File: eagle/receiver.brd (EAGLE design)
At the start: 68.6 x 53.3 mm, 15 parts, among them IC1 7805T, U1 ARDUINOR3-DIMENSION

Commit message: Better power management, improve usability
- LED strip pins reordered to match most strips
- Added a reset button
- Added a diode to protect the arduino from non-5vdc supplies
- Added a solder jumper to pick between sharing the arduino's 5vdc supply with
  the strip or whatever is on VCC
- Filter cap on regulator circuit
- Documentation silkscreens
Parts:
- added C1: (no value), adafruit:153CLV-0405
- added D1: (no value), adafruit:SMADIODE
- added JP7: (no value), SparkFun:1X02
- added RESET: (no value), SparkFun:TACTILE_SWITCH_SMD
- added U$4: (no value), phrobo:PHROBO-LOGO
- added U$5: (no value), ohw-logo:OSHW_FILLX150_NOTEXT
- added VCC/+5V: NC=+5v, SparkFun:SJ_2S-NO
- moved JP5 9.67 mm to (62.2, 20.3)
- moved JP3 7.73 mm to (62.2, 25.4)
- moved JP4 7.73 mm to (54.6, 25.4)
- moved JP6 7.41 mm to (54.6, 20.3)
- moved JP1 4.02 mm to (62.2, 15.2)
- moved JP2 4.02 mm to (54.6, 15.2)
- moved CLOCK 3.81 mm to (3.81, 47.0)
- moved DATA 3.81 mm to (3.81, 43.2)
- flipped VCC to the top, turned to 270 degrees
- renumbered 5V to +5V/VCC, U$1 to +5V, U$2 to VCC, U$3 to XBEE
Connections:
- removed net 5V: U1.5V
- new net N$4: RESET.4, U1.RESET, XBEE.5
- new net N$7: JP7.1, U1.5V
- new net N$8: +5V/VCC.1, D1.C, VCC/+5V.2
- net GND: now also C1.-, JP7.2, RESET.1, VCC.P$1; no longer VCC.P$2
- net N$1: now also VCC.P$2, VCC/+5V.1; no longer +5V.VCC, VCC.P$1
- net VCC: now also +5V.VCC, C1.+, D1.A; no longer +5V/VCC.1
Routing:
- net N$4: track 0.00 -> 73.9 mm
- net GND: track 132.9 -> 185.2 mm, vias 2 -> 3
- net N$7: track 0.00 -> 27.9 mm, vias 0 -> 1
- net N$8: track 0.00 -> 11.6 mm
- net N$1: track 50.2 -> 59.0 mm, vias 0 -> 3
- net N$3: track 35.3 -> 31.5 mm
- net N$2: track 36.6 -> 40.4 mm, vias 0 -> 2
- net VCC: track 100.3 -> 101.1 mm, vias 1 -> 0
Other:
- board text added: "(C)2015 Phong Robotics"
- board text added: "+5v ONLY"
- board text added: "5v"
- board text added: "Gnd"
- board text added: "Graviton Pokable - 1.0"
- board text added: "OHL v1.0"
- board text added: "[BL-1] Brilliance Linear (R1)"
- board text added: "http://phrobo.net/BL-1"

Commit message: Docs++
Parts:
- C1: value (none) -> 220uF; device adafruit:153CLV-0405 -> phrobo:UWT0J221MCL1GB
- moved C1 2.84 mm to (45.7, 11.4), turned to 270 degrees
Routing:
- net GND: track 185.2 -> 189.2 mm
- net VCC: track 101.1 -> 103.6 mm
- net N$7: track 27.9 -> 26.8 mm
- net N$1: track 59.0 -> 59.6 mm, vias 3 -> 2
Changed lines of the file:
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@@
 </class>
 </classes>
-<designrules name="default">
-<description language="en">&lt;b&gt;EAGLE Design Rules&lt;/b&gt;
+<designrules name="LaenPCBOrder">
+<description language="de">&lt;b&gt;EAGLE Design Rules&lt;/b&gt;
 &lt;p&gt;
-The default Design Rules have been set to cover
-a wide range of applications. Your particular design
-may have different requirements, so please make the
-necessary adjustments and save your customized
-design rules under a new name.
-</description>
+Die Standard-Design-Rules sind so gewählt, dass sie für
+die meisten Anwendungen passen. Sollte ihre Platine
+besondere Anforderungen haben, treffen Sie die erforderlichen
+Einstellungen hier und speichern die Design Rules unter
+einem neuen Namen ab.</description>
+<description language="en">&lt;b&gt;Laen's PCB Order Design Rules&lt;/b&gt;
+&lt;p&gt;
+Please make sure your boards conform to these design rules.</description>
 <param name="layerSetup" value="(1*16)"/>
-<param name="mtCopper" value="0.035mm 0.035mm 0.035mm 0.035mm 0.035mm 0.035mm 0.035mm 0.035mm 0.035mm 0.035mm 0.035mm 0.035mm 0.035mm 0.035mm 0.035mm 0.035mm"/>
-<param name="mtIsolate" value="1.5mm 0.15mm 0.2mm 0.15mm 0.2mm 0.15mm 0.2mm 0.15mm 0.2mm 0.15mm 0.2mm 0.15mm 0.2mm 0.15mm 0.2mm"/>
-<param name="mdWireWire" value="8mil"/>
-<param name="mdWirePad" value="8mil"/>
-<param name="mdWireVia" value="8mil"/>
-<param name="mdPadPad" value="8mil"/>
-<param name="mdPadVia" value="8mil"/>
-<param name="mdViaVia" value="8mil"/>
-<param name="mdSmdPad" value="8mil"/>
-<param name="mdSmdVia" value="8mil"/>
-<param name="mdSmdSmd" value="8mil"/>
+<param name="mtCopper" value="0.0356mm 0.0356mm 0.0356mm 0.0356mm 0.0356mm 0.0356mm 0.0356mm 0.0356mm 0.0356mm 0.0356mm 0.0356mm 0.0356mm 0.0356mm 0.0356mm 0.0356mm 0.0356mm"/>
+<param name="mtIsolate" value="1.5011mm 0.1499mm 0.2007mm 0.1499mm 0.2007mm 0.1499mm 0.2007mm 0.1499mm 0.2007mm 0.1499mm 0.2007mm 0.1499mm 0.2007mm 0.1499mm 0.2007mm"/>
+<param name="mdWireWire" value="6mil"/>
+<param name="mdWirePad" value="6mil"/>
+<param name="mdWireVia" value="6mil"/>
+<param name="mdPadPad" value="6mil"/>
+<param name="mdPadVia" value="6mil"/>
+<param name="mdViaVia" value="6mil"/>
+<param name="mdSmdPad" value="6mil"/>
+<param name="mdSmdVia" value="6mil"/>
+<param name="mdSmdSmd" value="6mil"/>
 <param name="mdViaViaSameLayer" value="8mil"/>
 <param name="mnLayersViaInSmd" value="2"/>
-<param name="mdCopperDimension" value="40mil"/>
-<param name="mdDrill" value="8mil"/>
+<param name="mdCopperDimension" value="15mil"/>
+<param name="mdDrill" value="6mil"/>
 <param name="mdSmdStop" value="0mil"/>
-<param name="msWidth" value="10mil"/>
-<param name="msDrill" value="0.6mm"/>
-<param name="msMicroVia" value="9.99mm"/>
+<param name="msWidth" value="6mil"/>
+<param name="msDrill" value="13mil"/>
+<param name="msMicroVia" value="13mil"/>
 <param name="msBlindViaRatio" value="0.5"/>
 <param name="rvPadTop" value="0.25"/>
@@
 <param name="rvMicroViaOuter" value="0.25"/>
 <param name="rvMicroViaInner" value="0.25"/>
-<param name="rlMinPadTop" value="10mil"/>
+<param name="rlMinPadTop" value="7mil"/>
 <param name="rlMaxPadTop" value="20mil"/>
-<param name="rlMinPadInner" value="10mil"/>
+<param name="rlMinPadInner" value="7mil"/>
 <param name="rlMaxPadInner" value="20mil"/>
-<param name="rlMinPadBottom" value="10mil"/>
+<param name="rlMinPadBottom" value="7mil"/>
 <param name="rlMaxPadBottom" value="20mil"/>
-<param name="rlMinViaOuter" value="8mil"/>
+<param name="rlMinViaOuter" value="7mil"/>
 <param name="rlMaxViaOuter" value="20mil"/>
-<param name="rlMinViaInner" value="8mil"/>
+<param name="rlMinViaInner" value="7mil"/>
 <param name="rlMaxViaInner" value="20mil"/>
 <param name="rlMinMicroViaOuter" value="4mil"/>
@@
 <param name="mvStopFrame" value="1"/>
 <param name="mvCreamFrame" value="0"/>
-<param name="mlMinStopFrame" value="4mil"/>
-<param name="mlMaxStopFrame" value="4mil"/>
+<param name="mlMinStopFrame" value="3mil"/>
+<param name="mlMaxStopFrame" value="3mil"/>
 <param name="mlMinCreamFrame" value="0mil"/>
 <param name="mlMaxCreamFrame" value="0mil"/>
@@
 <param name="checkRestrict" value="1"/>
 <param name="useDiameter" value="13"/>
-<param name="maxErrors" value="999999"/>
+<param name="maxErrors" value="50"/>
 </designrules>
 <autorouter>
@@
 <element name="RESET" library="SparkFun" package="TACTILE_SWITCH_SMD" value="" x="7.62" y="7.62"/>
 <element name="JP7" library="SparkFun" package="1X02" value="" x="49.53" y="21.59" rot="R270"/>
-<element name="C1" library="adafruit" package="153CLV-0405" value="" x="44.45" y="13.97"/>
+<element name="C1" library="phrobo" package="UWT0J221MCL1GB" value="220uF" x="45.72" y="11.43" rot="R270"/>
 <element name="D1" library="adafruit" package="SMADIODE" value="" x="10.16" y="43.18" rot="R270"/>
 <element name="U$4" library="phrobo" package="PHROBO-LOGO" value="" x="45.72" y="46.99"/>
@@
 <contactref element="C1" pad="-"/>
 <via x="44.45" y="19.05" extent="1-16" drill="0.6" shape="square"/>
-<wire x1="44.45" y1="19.05" x2="42.65" y2="19.05" width="0.6096" layer="1"/>
-<wire x1="42.65" y1="19.05" x2="42.65" y2="13.97" width="0.6096" layer="1"/>
-<wire x1="42.65" y1="13.97" x2="42.65" y2="5.61" width="0.6096" layer="1"/>
-<wire x1="42.65" y1="5.61" x2="44.45" y2="3.81" width="0.6096" layer="1"/>
 <wire x1="51.07" y1="33.71" x2="51.07" y2="33.02" width="0.6096" layer="1"/>
 <wire x1="51.07" y1="33.02" x2="48.26" y2="33.02" width="0.6096" layer="1"/>
@@
 <wire x1="44.45" y1="33.02" x2="44.45" y2="42.545" width="0.6096" layer="16"/>
 <via x="44.45" y="42.545" extent="1-16" drill="0.6" shape="square"/>
+<wire x1="41.22" y1="11.43" x2="41.22" y2="19.05" width="0.4064" layer="1"/>
+<wire x1="41.22" y1="19.05" x2="44.45" y2="19.05" width="0.4064" layer="1"/>
+<wire x1="44.45" y1="3.81" x2="44.45" y2="11.43" width="0.4064" layer="1"/>
+<wire x1="44.45" y1="11.43" x2="41.22" y2="11.43" width="0.4064" layer="1"/>
 </signal>
 <signal name="N$1">
@@
 <wire x1="13.97" y1="50.8" x2="13.97" y2="45.72" width="0.6096" layer="1"/>
 <via x="13.97" y="45.72" extent="1-16" drill="0.6" shape="square"/>
-<wire x1="13.97" y1="45.72" x2="36.83" y2="45.72" width="0.6096" layer="16"/>
-<via x="36.83" y="45.72" extent="1-16" drill="0.6" shape="square"/>
-<wire x1="36.83" y1="45.72" x2="36.83" y2="39.37" width="0.6096" layer="1"/>
 <wire x1="57.56" y1="46.355" x2="36.83" y2="46.355" width="0.6096" layer="16"/>
-<wire x1="36.83" y1="46.355" x2="36.83" y2="45.72" width="0.6096" layer="1"/>
+<wire x1="13.97" y1="45.72" x2="13.97" y2="46.355" width="0.4064" layer="16"/>
+<wire x1="13.97" y1="46.355" x2="36.83" y2="46.355" width="0.4064" layer="16"/>
 <via x="36.83" y="46.355" extent="1-16" drill="0.6" shape="square"/>
+<wire x1="36.83" y1="46.355" x2="36.83" y2="39.37" width="0.4064" layer="1"/>
 </signal>
 <signal name="VCC">
@@
 <contactref element="U1" pad="VIN"/>
 <contactref element="C1" pad="+"/>
-<wire x1="46.99" y1="13.97" x2="46.99" y2="3.81" width="0.6096" layer="1"/>
-<wire x1="46.25" y1="13.97" x2="46.99" y2="13.97" width="0.6096" layer="1"/>
-<wire x1="46.99" y1="13.97" x2="46.99" y2="39.37" width="0.6096" layer="1"/>
+<wire x1="46.99" y1="11.43" x2="46.99" y2="3.81" width="0.6096" layer="1"/>
+<wire x1="50.22" y1="11.43" x2="46.99" y2="11.43" width="0.6096" layer="1"/>
+<wire x1="46.99" y1="11.43" x2="46.99" y2="39.37" width="0.6096" layer="1"/>
 <wire x1="46.99" y1="39.37" x2="41.91" y2="39.37" width="0.6096" layer="1"/>
 <wire x1="9.74" y1="36.4" x2="9.74" y2="34.29" width="0.6096" layer="16"/>
@@
 <wire x1="49.53" y1="21.59" x2="45.72" y2="21.59" width="0.6096" layer="16"/>
 <via x="45.72" y="21.59" extent="1-16" drill="0.6" shape="square"/>
-<wire x1="45.72" y1="21.59" x2="39.37" y2="21.59" width="0.6096" layer="1"/>
-<wire x1="39.37" y1="21.59" x2="39.37" y2="3.81" width="0.6096" layer="1"/>
+<wire x1="45.72" y1="21.59" x2="39.37" y2="20.32" width="0.6096" layer="1"/>
+<wire x1="39.37" y1="20.32" x2="39.37" y2="3.81" width="0.6096" layer="1"/>
 </signal>
 <signal name="N$8">
@@
 </signal>
 </signals>
+<errors>
+</errors>
 </board>
 </drawing>

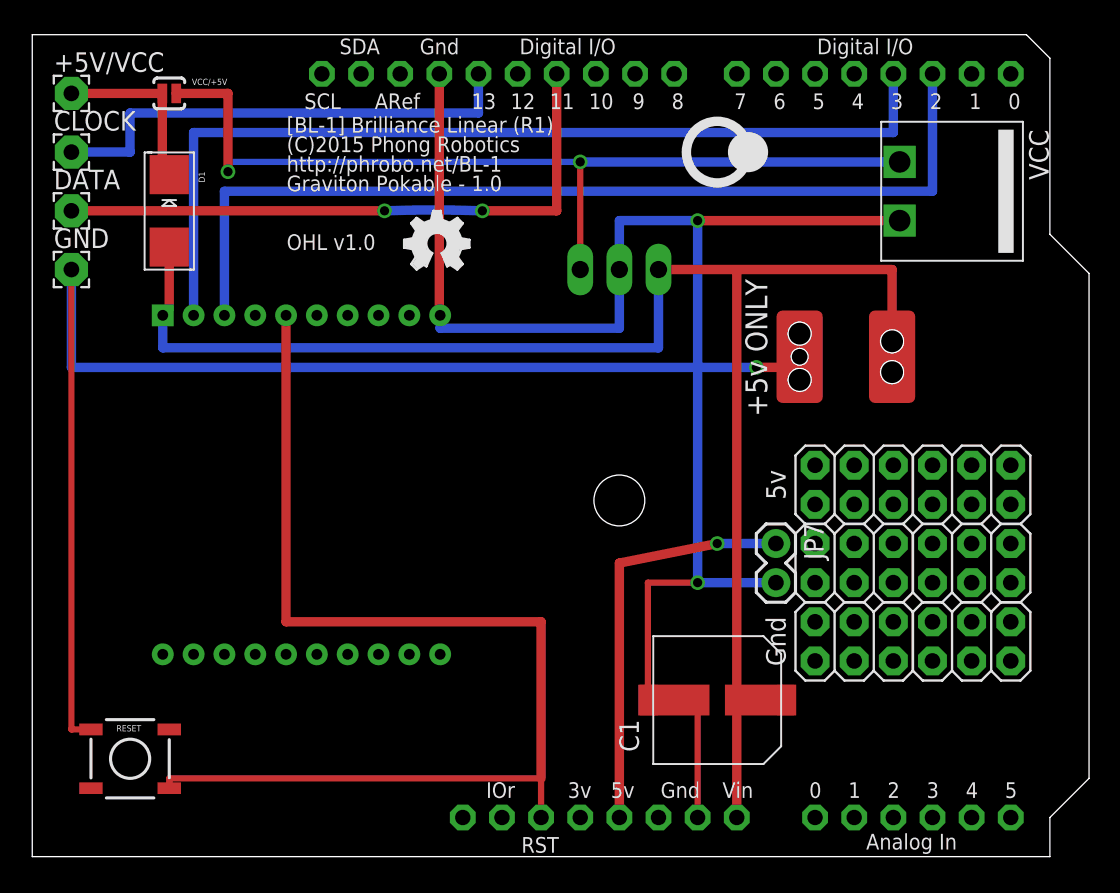
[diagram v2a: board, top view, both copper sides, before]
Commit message: Unflip flipped parts
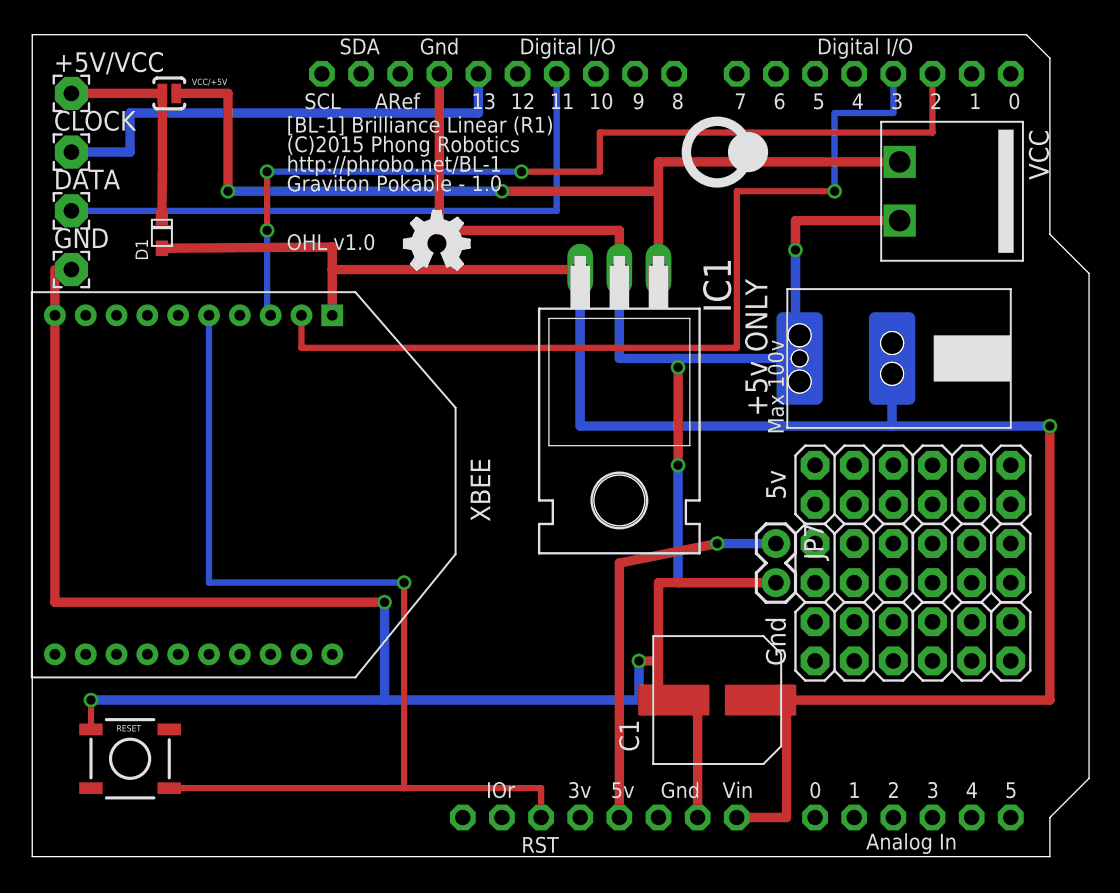
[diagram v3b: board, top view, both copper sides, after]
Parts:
- D1: device adafruit:SMADIODE -> adafruit:SOD-323F
- moved +5V 8.89 mm to (64.8, 38.1), flipped to the top, turned to 180 degrees
- moved D1 1.51 mm to (9.68, 41.8), turned to 90 degrees
- flipped IC1 to the top
- flipped XBEE to the top
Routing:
- net VCC: track 103.6 -> 122.3 mm, vias 0 -> 1
- net GND: track 189.2 -> 196.5 mm, vias 3 -> 6
- net N$4: track 73.9 -> 69.4 mm, vias 0 -> 1
- net N$6: track 61.1 -> 58.3 mm, vias 0 -> 1
- net N$5: track 61.6 -> 59.1 mm, vias 0 -> 3
- net N$8: track 11.6 -> 13.9 mm
- net N$1: track 59.6 -> 60.3 mm
- net N$2: vias 2 -> 0
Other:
- board text added: "Max 100v"
